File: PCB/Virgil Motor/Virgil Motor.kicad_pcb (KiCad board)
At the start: 2 copper layers, 20 x 107.5 mm, 14 parts, among them J1 10056847-101LF, J2 Conn_01x04_Pin, U1 B103, U2 DRV8220DSG, U3 IQS227B00400008TSR, U5 XIAO-RP2350-SMD

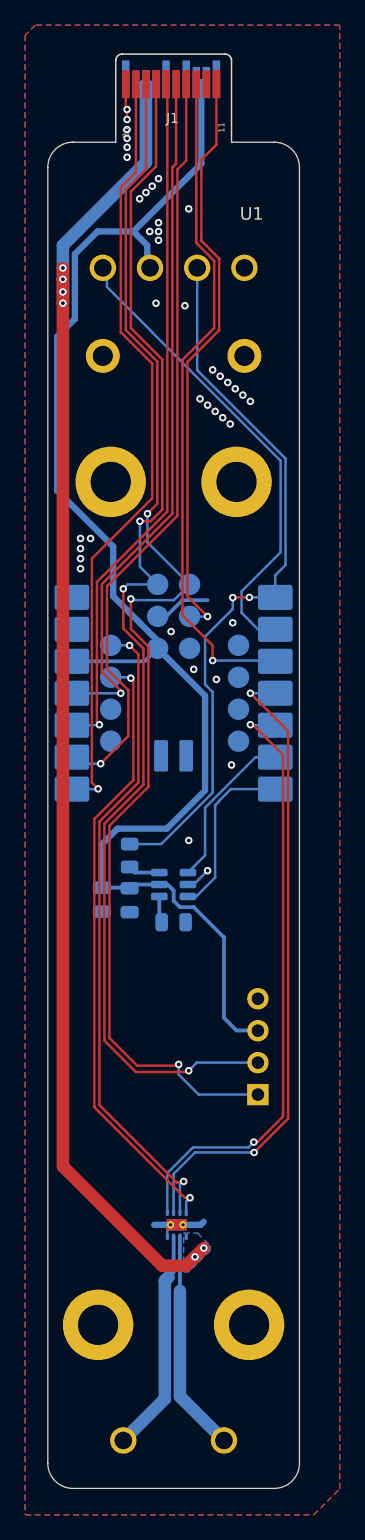
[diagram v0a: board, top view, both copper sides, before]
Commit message: Updated PCBs to use raw rp2040s
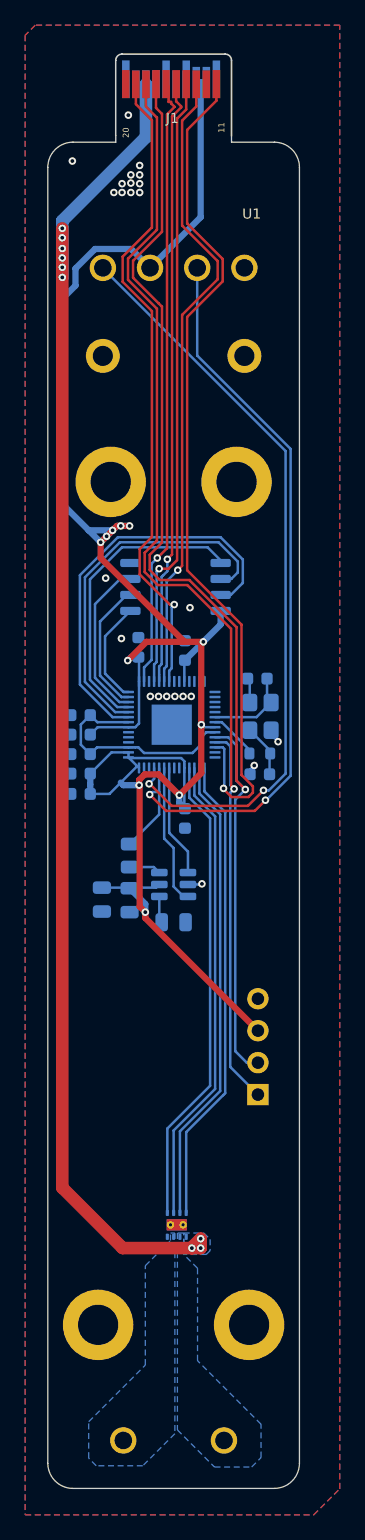
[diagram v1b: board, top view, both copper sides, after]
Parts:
- added C10: 100nF, Capacitor_SMD:C_0603_1608Metric, B.Cu at (148.9, 88.8)
- added C11: 100nF, Capacitor_SMD:C_0603_1608Metric, B.Cu at (148.9, 75.4)
- added C14: 22pF, Capacitor_SMD:C_0603_1608Metric, B.Cu at (154.7, 77.6)
- added C15: 22pF, Capacitor_SMD:C_0603_1608Metric, B.Cu at (154.8, 85.2)
- added C4: 100nF, Capacitor_SMD:C_0603_1608Metric, B.Cu at (140.6, 80.5)
- added C5: 100nF, Capacitor_SMD:C_0603_1608Metric, B.Cu at (140.6, 83.6)
- added C6: 100nF, Capacitor_SMD:C_0603_1608Metric, B.Cu at (140.6, 82.1)
- added C7: 100nF, Capacitor_SMD:C_0603_1608Metric, B.Cu at (140.6, 85.2)
- added C8: 100nF, Capacitor_SMD:C_0603_1608Metric, B.Cu at (145.2, 75.2)
- added C9: 100nF, Capacitor_SMD:C_0603_1608Metric, B.Cu at (140.6, 86.8)
- added R2: 1kΩ, Resistor_SMD:R_0603_1608Metric, B.Cu at (154.8, 83.6)
- added U4: W25Q16JVSS, Package_SO:SOIC-8_5.3x5.3mm_P1.27mm, B.Cu at (148.2, 70.3)
- added Y1: Crystal_GND24, Crystal:Crystal_SMD_Abracon_ABM8G-4Pin_3.2x2.5mm, B.Cu at (154.9, 80.6)
- U5: value XIAO-RP2350-SMD -> RP2040; footprint Snapeda:XIAO-RP2350-SMD -> Package_DFN_QFN:QFN-56-1EP_7x7mm_P0.4mm_EP3.2x3.2mm
- moved U5 2.50 mm to (147.8, 81.3), turned to -90 degrees
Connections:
- U5 pad 1: /Touch -> +3.3V
- U5 pad 10: /MOSI -> +3.3V
- U5 pad 11: /MISO -> unconnected-(U5-GPIO8-Pad11)
- U5 pad 12: +3.3V -> unconnected-(U5-GPIO9-Pad12)
- U5 pad 13: GND -> unconnected-(U5-GPIO10-Pad13)
- U5 pad 15: /Motor_MODE -> unconnected-(U5-GPIO12-Pad15)
- U5 pad 16: /Mtr_SLP -> unconnected-(U5-GPIO13-Pad16)
- U5 pad 2: /Wiper -> /MOSI
- U5 pad 20: unconnected-(U5-GPIO12_D16_SPI1_RX-Pad20) -> Net-(U5-XIN)
- U5 pad 21: unconnected-(U5-GPIO10_D17_SPI1_SCK-Pad21) -> Net-(U5-XOUT)
- U5 pad 22: unconnected-(U5-GPIO9_D18_SPI1_CS-Pad22) -> +3.3V
- U5 pad 23: /SWDIO -> +1V1
- U5 pad 25: /~{RST} -> /SWDIO
- U5 pad 26: GND -> /~{RST}
- U5 pad 28: +3.3V -> unconnected-(U5-GPIO17-Pad28)
- U5 pad 29: unconnected-(U5-BAT-Pad29) -> /Mtr_SLP
- U5 pad 3: /~{FlashCS} -> unconnected-(U5-GPIO1-Pad3)
- U5 pad 30: GND -> /Motor_MODE
- U5 pad 4: /PH -> /CLK
- U5 pad 5: /EN -> /MISO
- U5 pad 6: /Touch_DET -> /~{FlashCS}
- U5 pad 7: /Prox_DET -> /~{INT}
- U5 pad 8: /~{INT} -> unconnected-(U5-GPIO6-Pad8)
- U5 pad 9: /CLK -> unconnected-(U5-GPIO7-Pad9)
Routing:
- net +3.3V: track 114.0 -> 162.0 mm, vias 0 -> 11
- net /QSPI_SD3: track 0.00 -> 32.6 mm
- net /QSPI_SCLK: track 0.00 -> 29.1 mm
- net /QSPI_SD0: track 0.00 -> 24.0 mm
- net /Wiper: track 37.8 -> 60.3 mm, vias 0 -> 2
- net /~{RST}: track 46.5 -> 68.5 mm
- net +1V1: track 0.00 -> 18.3 mm
- net /M-: track 17.8 -> 0.00 mm
- net /M+: track 17.6 -> 0.00 mm
- net /Motor_MODE: track 51.6 -> 37.4 mm, vias 2 -> 0
- net /PH: track 51.0 -> 37.4 mm, vias 2 -> 0
- net /QSPI_SD2: track 0.00 -> 13.0 mm
- net /CLK: track 60.7 -> 49.0 mm
- net /Mtr_SLP: track 49.0 -> 37.3 mm, vias 2 -> 0
- net /EN: track 48.6 -> 37.5 mm, vias 2 -> 0
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- added copper zone on B.Cu, net /M+
- added copper zone on B.Cu, net /M-

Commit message: Finished PCBs
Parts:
- Y1: value Crystal_GND24 -> ABM8-272-T3
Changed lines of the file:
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@@
 	)
 	(footprint "Snapeda:B103"
-		(locked yes)
 		(layer "F.Cu")
 		(at 148 108.638172 -90)
@@
 			)
 		)
-		(attr smd)
+		(attr smd dnp)
 		(duplicate_pad_numbers_are_jumpers no)
 		(fp_rect
@@
 			)
 		)
-		(attr smd)
+		(attr smd dnp)
 		(duplicate_pad_numbers_are_jumpers no)
 		(fp_line
@@
 			)
 		)
-		(property "Value" "Crystal_GND24"
+		(property "Value" "ABM8-272-T3"
 			(at 0 -2.45 90)
 			(layer "B.Fab")

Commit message: Added Images to readme
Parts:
- removed C1, C3: 1uF, Capacitor_SMD:C_0805_2012Metric
- removed C2: 100pF, Capacitor_SMD:C_0805_2012Metric
- removed R1: 470Ω, Resistor_SMD:R_0805_2012Metric
- C14, C15: value 22pF -> 15pF
- U3: value IQS227B00400008TSR -> CAP1293-1-SN-TR; footprint Package_TO_SOT_SMD:TSOT-23-6 -> Snapeda:SOIC8_4P9X3P9MC_MCH-L
- moved U3 1.61 mm to (147.2, 95.4), turned to -90 degrees
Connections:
- net /Prox_DET renamed /SCL
- U3 pad 1: /Touch_DET -> /Touch_INT
- U3 pad 2: GND -> /SDA
- U3 pad 4: Net-(U3-VREG) -> +3.3V
- U3 pad 5: +3.3V -> GND
- U3 pad 6: Net-(U3-CX) -> /Touch
- U5 pad 35: unconnected-(U5-GPIO23-Pad35) -> /Touch_INT
- U5 pad 36: /Touch_DET -> /SDA
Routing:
- net /Touch_INT: track 0.00 -> 10.2 mm, vias 0 -> 2
- net /SDA: track 0.00 -> 9.89 mm, vias 0 -> 2
- net /Touch: track 64.2 -> 73.3 mm
- net /Touch_DET: track 8.93 -> 0.00 mm
- net Net-(U3-CX): track 2.54 -> 0.00 mm
- net +3.3V: track 162.0 -> 159.9 mm
- net Net-(U3-VREG): track 2.13 -> 0.00 mm
- net /SCL: track 11.2 -> 9.28 mm
- net GND: track 5.08 -> 3.95 mm, vias 24 -> 23
